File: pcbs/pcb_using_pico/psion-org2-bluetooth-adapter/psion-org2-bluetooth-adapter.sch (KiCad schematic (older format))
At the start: 24 parts, among them J1 Conn_02x08_Odd_Even, J5 Conn_01x04_Female, J7 Conn_01x03_Female, M2 Si2301, U1 74LS245, U2 74LS245, U3 Pico

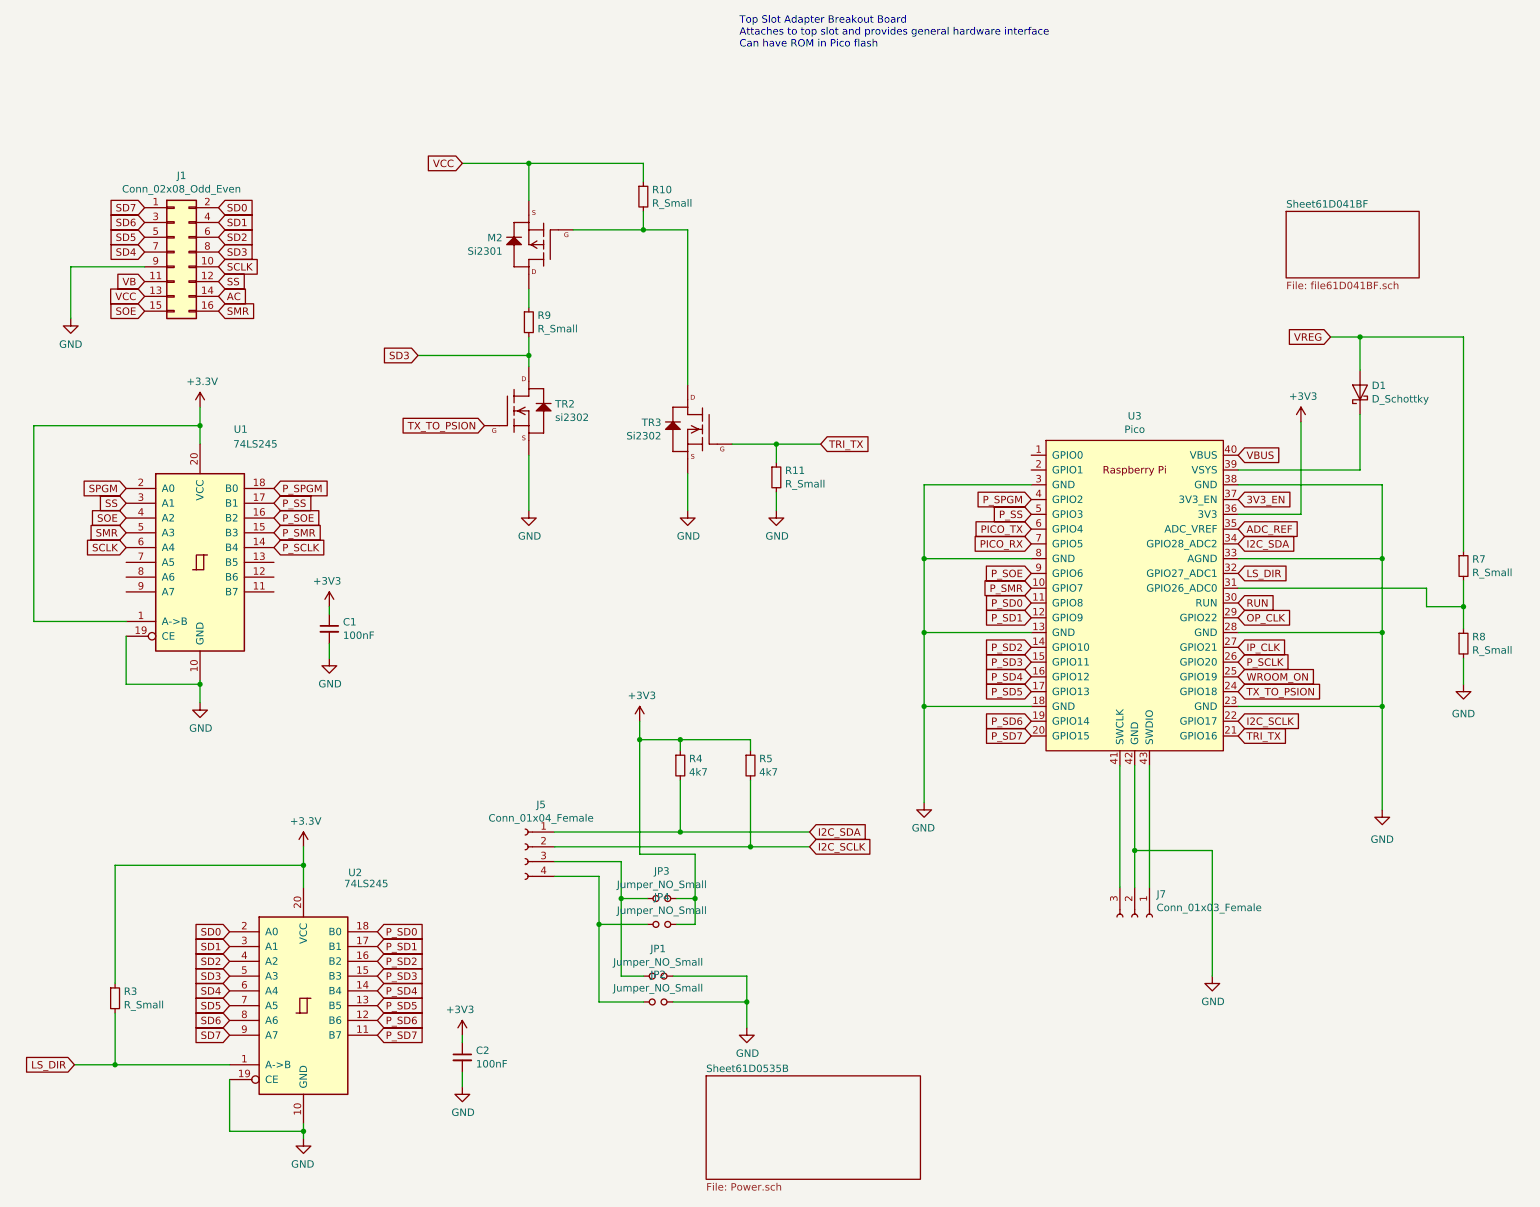
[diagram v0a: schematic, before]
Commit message: V2.0 sent off for fab. New charger IC with more solderable footprint, plus other fixes
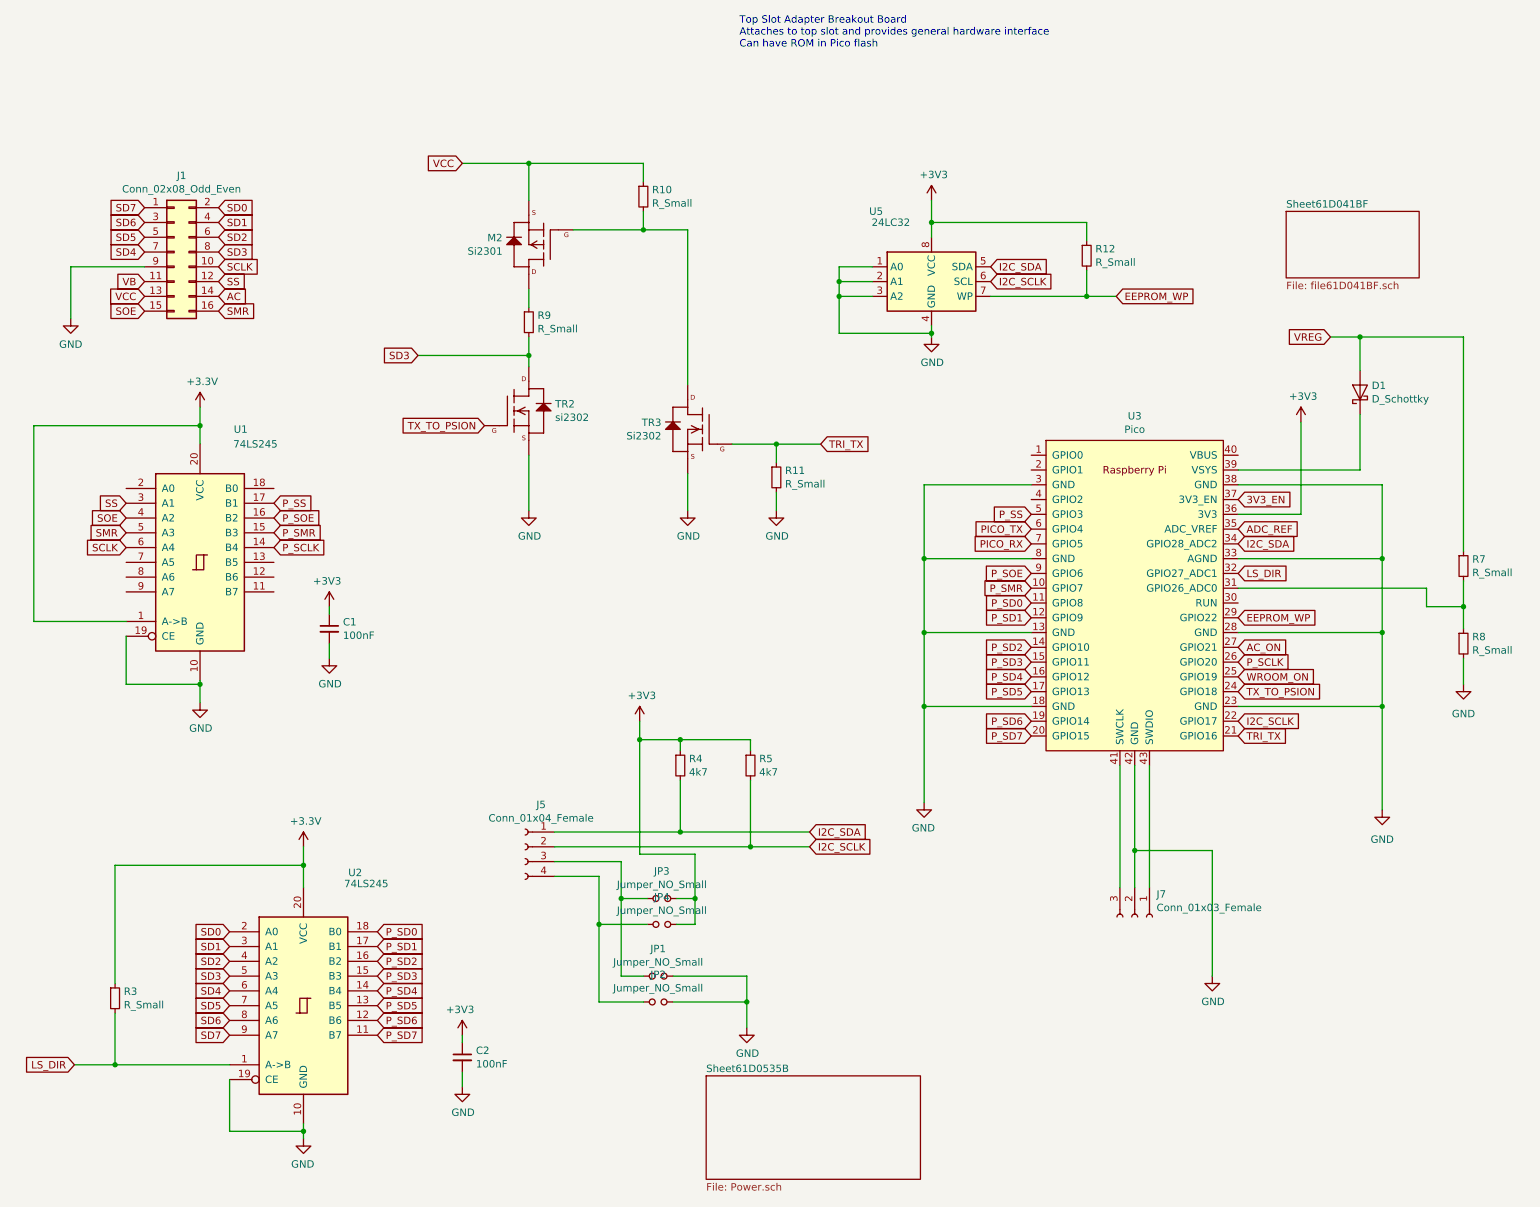
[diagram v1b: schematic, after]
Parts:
- added R12: R_Small, Resistor_SMD:R_0805_2012Metric, symbol Device:R_Small
- added U5: 24LC32, Package_SO:SOIC-8_3.9x4.9mm_P1.27mm, symbol Memory_EEPROM:24LC32
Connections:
- net +3V3: now also R12.1, U5.8 (VCC)
- net GND: now also U5.1 (A0), U5.2 (A1), U5.3 (A2), U5.4 (GND)
- net I2C_SCLK: now also U5.6 (SCL)
- net I2C_SDA: now also U5.5 (SDA)
- net IP_CLK renamed AC_ON
- net OP_CLK renamed EEPROM_WP
- net EEPROM_WP: now also R12.2, U5.7 (WP)
- net P_SPGM: no longer names the net of U3.4 (GPIO2)
- net P_SPGM: no longer U1.18 (B0)
- net RUN: no longer names the net of U3.30 (RUN)
- net SPGM: no longer names the net of U1.2 (A0)
- net VBUS: no longer names the net of U3.40 (VBUS)
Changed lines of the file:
@@
 Text GLabel 1300 2875 0    50   Input ~ 0
 SS
-Text GLabel 1300 2775 0    50   Input ~ 0
-SPGM
 Text GLabel 1925 1375 2    50   Input ~ 0
 SS
@@
 Text GLabel 1925 1075 2    50   Input ~ 0
 SD2
-Text GLabel 7425 2850 0    50   Input ~ 0
-P_SPGM
 Text GLabel 7425 2950 0    50   Input ~ 0
 P_SS
@@
 Text GLabel 2300 2875 2    50   Input ~ 0
 P_SS
-Text GLabel 2300 2775 2    50   Input ~ 0
-P_SPGM
 Wire Wire Line
 	3575 6525 3575 6475
@@
 Text GLabel 8825 3050 2    50   Input ~ 0
 ADC_REF
-Text GLabel 8825 3550 2    50   Input ~ 0
-RUN
-Text GLabel 8825 2550 2    50   Input ~ 0
-VBUS
 $Comp
 L 74xx:74LS245 U?
@@
 Text GLabel 1425 1375 0    50   Input ~ 0
 VB
-Text GLabel 8825 3850 2    50   Input ~ 0
-IP_CLK
-Text GLabel 8825 3650 2    50   Input ~ 0
-OP_CLK
 $Comp
 L power:GND #PWR0107
@@
 	6000 2475 5700 2475
 Connection ~ 5700 2475
+$Comp
+L Memory_EEPROM:24LC32 U5
+U 1 1 62133209
+P 6750 1375
+F 0 "U5" H 6375 1850 50  0000 C CNN
+F 1 "24LC32" H 6475 1775 50  0000 C CNN
+F 2 "Package_SO:SOIC-8_3.9x4.9mm_P1.27mm" H 6750 1375 50  0001 C CNN
+F 3 "http://ww1.microchip.com/downloads/en/DeviceDoc/21072G.pdf" H 6750 1375 50  0001 C CNN
+	1    6750 1375
+	1    0    0    -1
+$EndComp
+Text GLabel 7150 1375 2    50   Input ~ 0
+I2C_SCLK
+Text GLabel 7150 1275 2    50   Input ~ 0
+I2C_SDA
+$Comp
+L power:GND #PWR0138
+U 1 1 6213881D
+P 6750 1750
+F 0 "#PWR0138" H 6750 1500 50  0001 C CNN
+F 1 "GND" H 6755 1577 50  0000 C CNN
+F 2 "" H 6750 1750 50  0001 C CNN
+F 3 "" H 6750 1750 50  0001 C CNN
+	1    6750 1750
+	1    0    0    -1
+$EndComp
+Wire Wire Line
+	6750 1750 6750 1725
+$Comp
+L power:+3V3 #PWR0139
+U 1 1 6213CC87
+P 6750 825
+F 0 "#PWR0139" H 6750 675 50  0001 C CNN
+F 1 "+3V3" H 6765 998 50  0000 C CNN
+F 2 "" H 6750 825 50  0001 C CNN
+F 3 "" H 6750 825 50  0001 C CNN
+	1    6750 825
+	1    0    0    -1
+$EndComp
+Wire Wire Line
+	6750 825  6750 975
+Connection ~ 6750 1725
+Wire Wire Line
+	6750 1725 6750 1675
+Wire Wire Line
+	6750 1725 6125 1725
+Wire Wire Line
+	6125 1725 6125 1475
+Wire Wire Line
+	6125 1275 6350 1275
+Wire Wire Line
+	6350 1375 6125 1375
+Connection ~ 6125 1375
+Wire Wire Line
+	6125 1375 6125 1275
+Wire Wire Line
+	6350 1475 6125 1475
+Connection ~ 6125 1475
+Wire Wire Line
+	6125 1475 6125 1375
+$Comp
+L Device:R_Small R12
+U 1 1 62152431
+P 7800 1200
+F 0 "R12" H 7859 1246 50  0000 L CNN
+F 1 "R_Small" H 7859 1155 50  0000 L CNN
+F 2 "Resistor_SMD:R_0805_2012Metric" H 7800 1200 50  0001 C CNN
+F 3 "~" H 7800 1200 50  0001 C CNN
+	1    7800 1200
+	1    0    0    -1
+$EndComp
+Wire Wire Line
+	7800 1475 7800 1300
+Wire Wire Line
+	7150 1475 7800 1475
+Wire Wire Line
+	7800 1100 7800 975
+Wire Wire Line
+	7800 975  6750 975
+Connection ~ 6750 975
+Wire Wire Line
+	6750 975  6750 1075
+Text GLabel 8000 1475 2    50   Input ~ 0
+EEPROM_WP
+Wire Wire Line
+	8000 1475 7800 1475
+Connection ~ 7800 1475
+Text GLabel 8825 3650 2    50   Input ~ 0
+EEPROM_WP
+Text GLabel 8825 3850 2    50   Input ~ 0
+AC_ON
 $EndSCHEMATC

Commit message: Updates that stop the code from working. ROm read is problematic, not sure how demo worked.
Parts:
- R10, R11: value R_Small -> 10k
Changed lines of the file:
@@
 P 4800 800
 F 0 "R10" H 4859 846 50  0000 L CNN
-F 1 "R_Small" H 4859 755 50  0000 L CNN
+F 1 "10k" H 4859 755 50  0000 L CNN
 F 2 "Resistor_SMD:R_0805_2012Metric" H 4800 800 50  0001 C CNN
 F 3 "~" H 4800 800 50  0001 C CNN
@@
 P 5700 2700
 F 0 "R11" H 5759 2746 50  0000 L CNN
-F 1 "R_Small" H 5759 2655 50  0000 L CNN
+F 1 "10k" H 5759 2655 50  0000 L CNN
 F 2 "Resistor_SMD:R_0805_2012Metric" H 5700 2700 50  0001 C CNN
 F 3 "~" H 5700 2700 50  0001 C CNN

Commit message: These changes are a bluetooth adapter that doesn't use interrupts as that messes up the ROM load. The PIOs are used for two UARTS and no interrupts and not blocking. Two way comms sems to work The wireless code now runs on core 1 and the ROM load code runs on core 0. Error occurs on exit from TERM mode and a delay needed at startup of a few seconds.
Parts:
- added TR?: Si2302, Package_TO_SOT_SMD:SOT-23, symbol cq1re1-cache:New_Library_Si2302CDS-n-channel
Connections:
- net GND: now also TR?.2 (S); no longer TR2.2 (S)
- net TRI_TX: now also TR?.1 (G)
- new net: TR2.2 (S), TR?.3 (D)
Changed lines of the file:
@@
 L power:GND #PWR0135
 U 1 1 620A1225
-P 4025 2925
-F 0 "#PWR0135" H 4025 2675 50  0001 C CNN
-F 1 "GND" H 4030 2752 50  0000 C CNN
-F 2 "" H 4025 2925 50  0001 C CNN
-F 3 "" H 4025 2925 50  0001 C CNN
-	1    4025 2925
-	1    0    0    -1
-$EndComp
-Wire Wire Line
-	4025 2925 4025 2550
+P 4025 3625
+F 0 "#PWR0135" H 4025 3375 50  0001 C CNN
+F 1 "GND" H 4030 3452 50  0000 C CNN
+F 2 "" H 4025 3625 50  0001 C CNN
+F 3 "" H 4025 3625 50  0001 C CNN
+	1    4025 3625
+	1    0    0    -1
+$EndComp
 $Comp
 L Device:R_Small R9
@@
 $EndComp
 Wire Wire Line
-	5400 2475 5700 2475
+	5400 2475 5525 2475
 Wire Wire Line
 	5700 2475 5700 2600
@@
 Text GLabel 8825 3850 2    50   Input ~ 0
 AC_ON
+$Comp
+L cq1re1-cache:New_Library_Si2302CDS-n-channel TR?
+U 1 1 62319062
+P 4125 3025
+F 0 "TR?" H 4403 3071 50  0000 L CNN
+F 1 "Si2302" H 4403 2980 50  0000 L CNN
+F 2 "Package_TO_SOT_SMD:SOT-23" H 4155 3175 20  0001 C CNN
+F 3 "" H 4125 3025 50  0001 C CNN
+	1    4125 3025
+	-1   0    0    -1
+$EndComp
+Wire Wire Line
+	4025 2550 4025 2725
+Wire Wire Line
+	4025 3625 4025 3325
+Wire Wire Line
+	5525 2475 5525 3125
+Wire Wire Line
+	5525 3125 4325 3125
+Connection ~ 5525 2475
+Wire Wire Line
+	5525 2475 5700 2475
 $EndSCHEMATC
